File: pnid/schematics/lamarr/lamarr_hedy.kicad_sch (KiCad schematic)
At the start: 102 parts, among them U2 ox_sense_12V:sensor

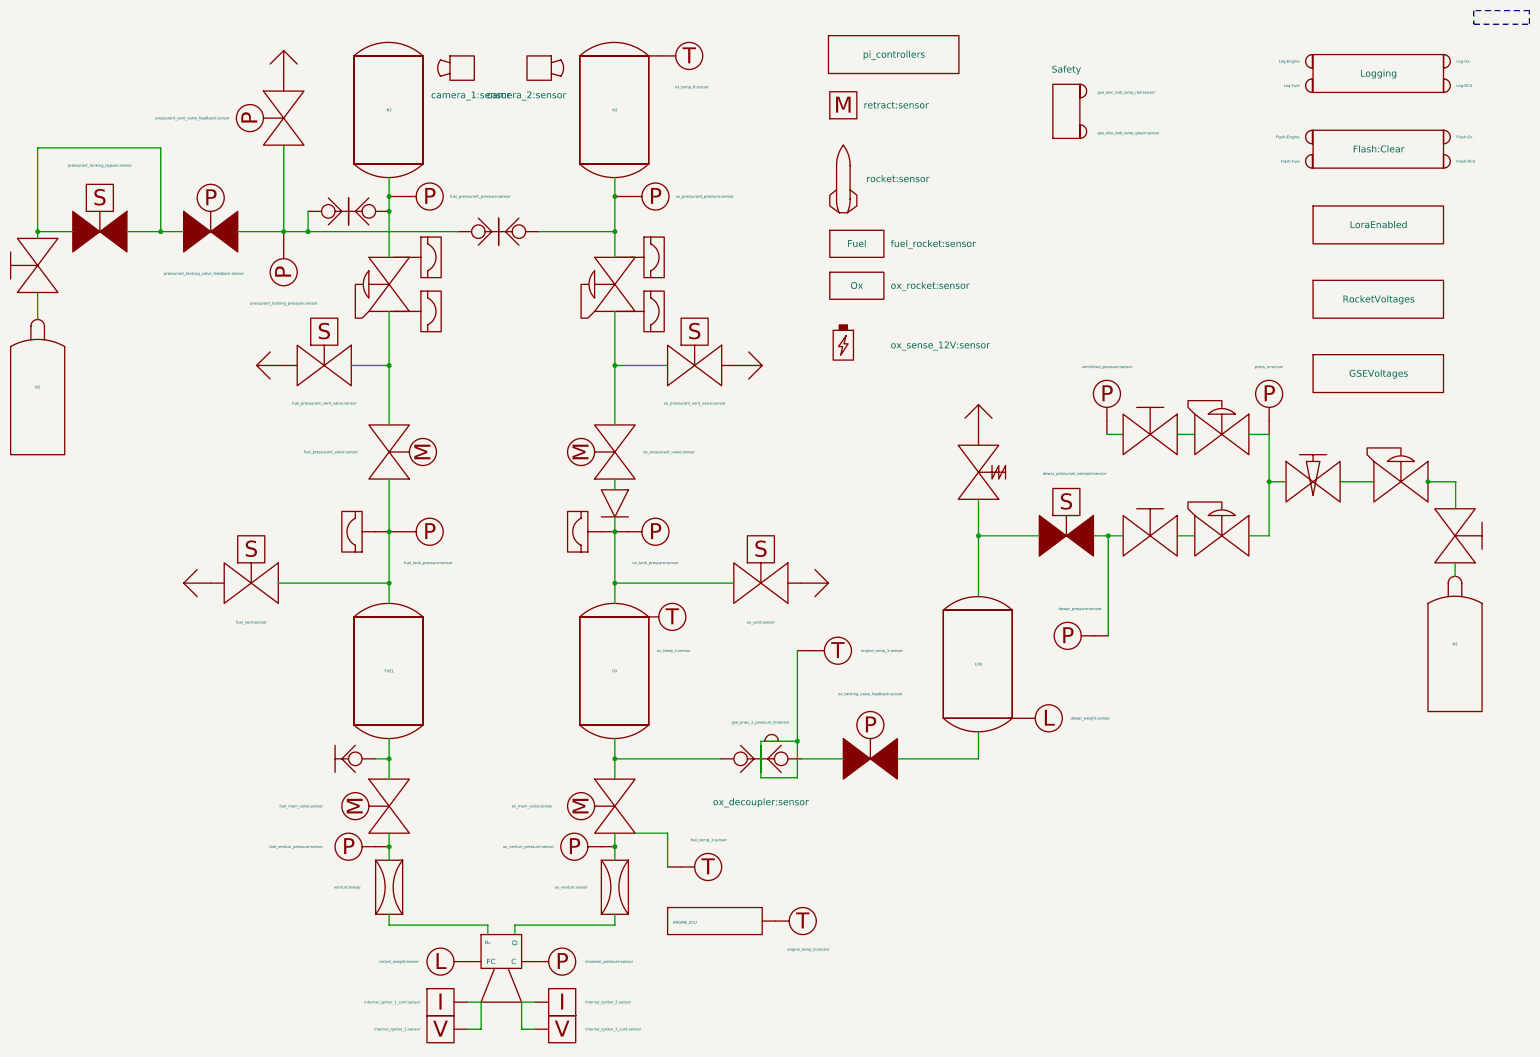
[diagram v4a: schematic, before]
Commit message: more refinements in sensor calibration & ECUI look
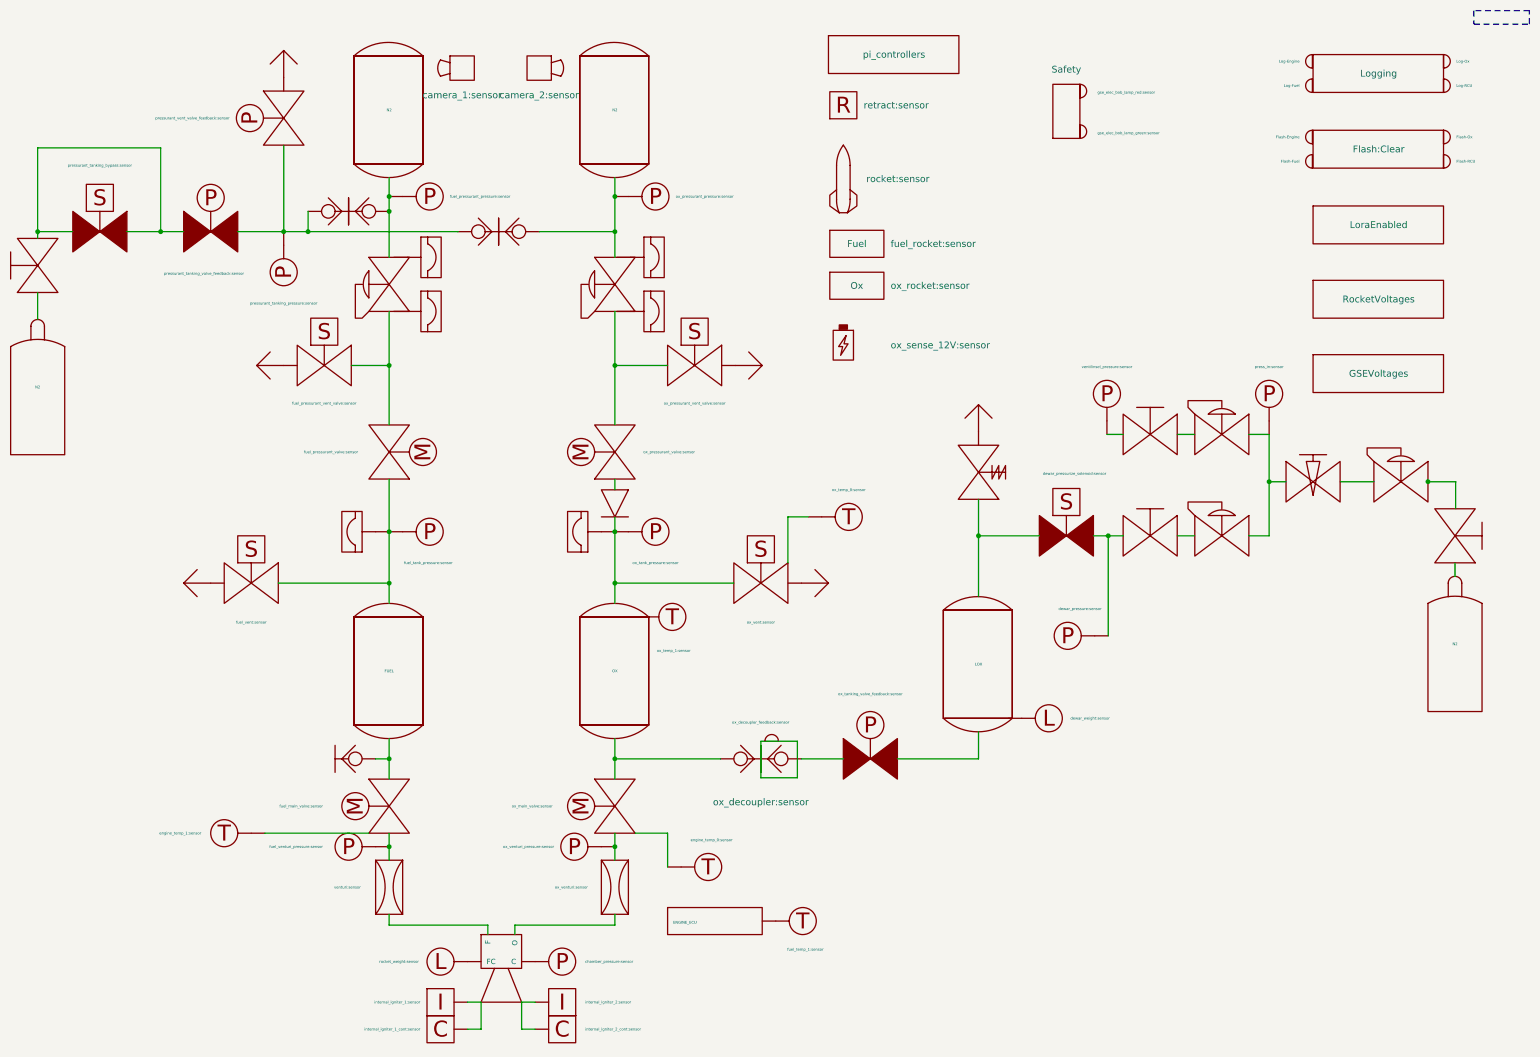
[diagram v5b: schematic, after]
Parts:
- Motor1: symbol PnID-Lib:Motor -> PnID-Lib:Retract
- engine_ECU_temperature: value engine_temp_0:sensor -> fuel_temp_1:sensor
- igniter1: value internal_igniter_1_cont:sensor -> internal_igniter_1:sensor; Unit Ohm -> mA
- igniter2: Unit Ohm -> mA
- igniter_1_continuity: renamed from voltmeter1; value internal_igniter_1:sensor -> internal_igniter_1_cont:sensor; symbol PnID-Lib:voltmeter -> PnID-Lib:continuity; Unit V -> (none)
- igniter_2_continuity: renamed from voltmeter2; symbol PnID-Lib:voltmeter -> PnID-Lib:continuity; Unit V -> (none)
- ox_decoupler_feedback: value gse_pneu_2_pressure_0:sensor -> ox_decoupler_feedback:sensor
- ox_main_valve_servo_temperature: value fuel_temp_1:sensor -> engine_temp_0:sensor
- renumbered ox_decoupler_temperature to fuel_main_valve_servo_temperature, ox_press_temp to ox_vent_temperature
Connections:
- net at engine.~ (C): now also venturi1.~; no longer ox_venturi.~
- net at venturi1.~: now also fuel_main_valve.~, fuel_venturi_pressure.~; no longer engine.~ (C)
- net at dewar_needle_valve?.~: now also C2.~, C3.~; no longer C1.~
- new net: engine.~ (C), ox_venturi.~
- new net: OX.~, ox_main_valve.~, ox_quick_connect.~
- new net: DewarOverPressureValve?.~, LOX.~, dewar_pressurize_solenoid.~
- new net: C1.~, dewar_needle_valve?.~
- new net: ox_pressurant_valve.~, ox_pressurant_vent_valve.~, pressurantPressureRegulator2.~
- new net: FUEL.~, fuel_main_valve.~, ox_quick_connect1.~
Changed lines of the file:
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@@
 	)
 	(junction
-		(at 155.194 151.892)
-		(diameter 0)
-		(color 0 0 0 0)
-	)
-	(junction
 		(at 78.486 81.28)
 		(diameter 0)
@@
 	(wire
 		(pts
+			(xy 153.416 109.728) (xy 157.226 109.728)
+		)
+		(stroke
+			(width 0)
+			(type default)
+		)
+	)
+	(wire
+		(pts
 			(xy 213.614 113.284) (xy 210.82 113.284)
 		)
@@
 	(wire
 		(pts
-			(xy 155.194 134.874) (xy 155.194 151.892)
-		)
-		(stroke
-			(width 0)
-			(type default)
-		)
-	)
-	(wire
-		(pts
 			(xy 189.23 113.284) (xy 189.23 124.714)
 		)
@@
 		)
 	)
+	(wire
+		(pts
+			(xy 153.416 118.364) (xy 153.416 109.728)
+		)
+		(stroke
+			(width 0)
+			(type default)
+		)
+	)
 	(polyline
 		(pts
@@
 	(wire
 		(pts
+			(xy 74.676 169.164) (xy 55.118 169.164)
+		)
+		(stroke
+			(width 0)
+			(type default)
+		)
+	)
+	(wire
+		(pts
 			(xy 12.4406 56.134) (xy 19.05 56.134)
 		)
@@
 			)
 		)
-		(property "Value" "internal_igniter_1_cont:sensor"
+		(property "Value" "internal_igniter_1:sensor"
 			(at 84.328 200.914 0)
 			(effects
@@
 			)
 		)
-		(property "Unit" "Ohm"
+		(property "Unit" "mA"
 			(at 88.138 200.914 0)
 			(effects
@@
 			)
 		)
-		(property "Unit" "Ohm"
+		(property "Unit" "mA"
 			(at 110.998 200.914 0)
 			(effects
@@
 	)
 	(symbol
-		(lib_id "PnID-Lib:Motor")
+		(lib_id "PnID-Lib:Retract")
 		(at 163.83 32.512 0)
 		(unit 1)
@@
 	(symbol
 		(lib_id "PnID-Lib:Sensor_Temperature")
-		(at 134.874 23.114 0)
+		(at 164.846 109.728 0)
 		(unit 1)
 		(exclude_from_sim no)
@@
 		(on_board yes)
 		(dnp no)
-		(property "Reference" "ox_press_temp"
-			(at 138.684 22.479 0)
+		(property "Reference" "ox_vent_temperature"
+			(at 168.656 109.093 0)
 			(effects
 				(font
@@
 		)
 		(property "Value" "ox_temp_0:sensor"
-			(at 135.382 28.956 0)
+			(at 164.846 104.648 0)
 			(effects
 				(font
@@
 		)
 		(property "Footprint" ""
-			(at 134.874 23.114 0)
+			(at 164.846 109.728 0)
 			(effects
 				(font
@@
 		)
 		(property "Datasheet" ""
-			(at 134.874 23.114 0)
+			(at 164.846 109.728 0)
 			(effects
 				(font
@@
 		)
 		(property "Description" ""
-			(at 134.874 23.114 0)
+			(at 164.846 109.728 0)
 			(effects
 				(font
@@
 		)
 		(property "Unit" "˚C"
-			(at 134.874 23.114 0)
+			(at 164.846 109.728 0)
 			(effects
 				(font
@@
 		)
 		(property "Action_Reference" " "
-			(at 134.874 23.114 0)
+			(at 164.846 109.728 0)
 			(effects
 				(font
@@
 			(project "lamarr_hedy"
 				(path "/604fc9f3-63a6-4133-afd1-4a5c2507dc1d"
-					(reference "ox_press_temp")
+					(reference "ox_vent_temperature")
 					(unit 1)
 				)
@@
 		)
 		(property "Value" "camera_2:sensor"
-			(at 111.76 30.48 0)
+			(at 106.68 30.48 0)
 			(effects
 				(font
 					(size 1.27 1.27)
 				)
-				(justify right)
 			)
 		)
@@
 	)
 	(symbol
-		(lib_id "PnID-Lib:voltmeter")
+		(lib_id "PnID-Lib:continuity")
 		(at 88.138 205.994 0)
 		(unit 1)
@@
 		(on_board yes)
 		(dnp no)
-		(property "Reference" "voltmeter1"
+		(property "Reference" "igniter_1_continuity"
 			(at 83.058 203.708 0)
 			(effects
@@
 			)
 		)
-		(property "Value" "internal_igniter_1:sensor"
+		(property "Value" "internal_igniter_1_cont:sensor"
 			(at 84.328 205.994 0)
 			(effects
@@
 			)
 		)
-		(property "Unit" "V"
+		(property "Unit" ""
 			(at 88.138 205.994 0)
 			(effects
@@
 			(project ""
 				(path "/604fc9f3-63a6-4133-afd1-4a5c2507dc1d"
-					(reference "voltmeter1")
+					(reference "igniter_1_continuity")
 					(unit 1)
 				)
@@
 			)
 		)
-		(property "Value" "fuel_temp_1:sensor"
+		(property "Value" "engine_temp_0:sensor"
 			(at 135.128 170.434 0)
 			(effects
@@
 			)
 		)
-		(property "Value" "gse_pneu_2_pressure_0:sensor"
+		(property "Value" "ox_decoupler_feedback:sensor"
 			(at 153.67 148.336 0)
 			(effects
@@
 	)
 	(symbol
-		(lib_id "PnID-Lib:voltmeter")
+		(lib_id "PnID-Lib:continuity")
 		(at 110.998 205.994 0)
 		(mirror y)
@@
 		(on_board yes)
 		(dnp no)
-		(property "Reference" "voltmeter2"
+		(property "Reference" "igniter_2_continuity"
 			(at 116.078 203.708 0)
 			(effects
@@
 			)
 		)
-		(property "Unit" "V"
+		(property "Unit" ""
 			(at 110.998 205.994 0)
 			(effects
@@
 			(project "lamarr_hedy"
 				(path "/604fc9f3-63a6-4133-afd1-4a5c2507dc1d"
-					(reference "voltmeter2")
+					(reference "igniter_2_continuity")
 					(unit 1)
 				)
@@
 			)
 		)
-		(property "Value" "engine_temp_0:sensor"
+		(property "Value" "fuel_temp_1:sensor"
 			(at 153.289 191.008 0)
 			(effects
@@
 		(lib_name "Sensor_Temperature_1")
 		(lib_id "PnID-Lib:Sensor_Temperature")
-		(at 162.814 134.874 0)
+		(at 47.498 169.164 180)
 		(unit 1)
 		(exclude_from_sim no)
@@
 		(on_board yes)
 		(dnp no)
-		(property "Reference" "ox_decoupler_temperature"
-			(at 166.624 134.239 0)
+		(property "Reference" "fuel_main_valve_servo_temperature"
+			(at 43.688 169.799 0)
 			(effects
 				(font
@@
 		)
 		(property "Value" "engine_temp_1:sensor"
-			(at 167.132 134.874 0)
+			(at 43.18 169.164 0)
 			(effects
 				(font
@@
 		)
 		(property "Footprint" ""
-			(at 162.814 134.874 0)
+			(at 47.498 169.164 0)
 			(effects
 				(font
@@
 		)
 		(property "Datasheet" ""
-			(at 162.814 134.874 0)
+			(at 47.498 169.164 0)
 			(effects
 				(font
@@
 		)
 		(property "Description" ""
-			(at 162.814 134.874 0)
+			(at 47.498 169.164 0)
 			(effects
 				(font
@@
 		)
 		(property "Unit" "˚C"
-			(at 162.814 134.874 0)
+			(at 47.498 169.164 0)
 			(effects
 				(font
@@
 		)
 		(property "Action_Reference" " "
-			(at 162.814 134.874 0)
+			(at 47.498 169.164 0)
 			(effects
 				(font
@@
 			(project "lamarr_hedy"
 				(path "/604fc9f3-63a6-4133-afd1-4a5c2507dc1d"
-					(reference "ox_decoupler_temperature")
+					(reference "fuel_main_valve_servo_temperature")
 					(unit 1)
 				)
@@
 		)
 		(property "Value" "camera_1:sensor"
-			(at 86.36 30.48 0)
+			(at 92.202 30.48 0)
 			(effects
 				(font
 					(size 1.27 1.27)
 				)
-				(justify right)
 			)
 		)
